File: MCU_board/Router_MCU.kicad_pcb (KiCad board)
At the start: 2 copper layers, 99 x 84.5 mm, 72 parts, among them J1 Header, T1 HY601742, U1 MYC-YT507H, U2 TPS54340, U3 LAN8720A, X1 B4B-XH, X2 B4B-XH, X3 B4B-XH, X4 B4B-XH, X5 B2B-XH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

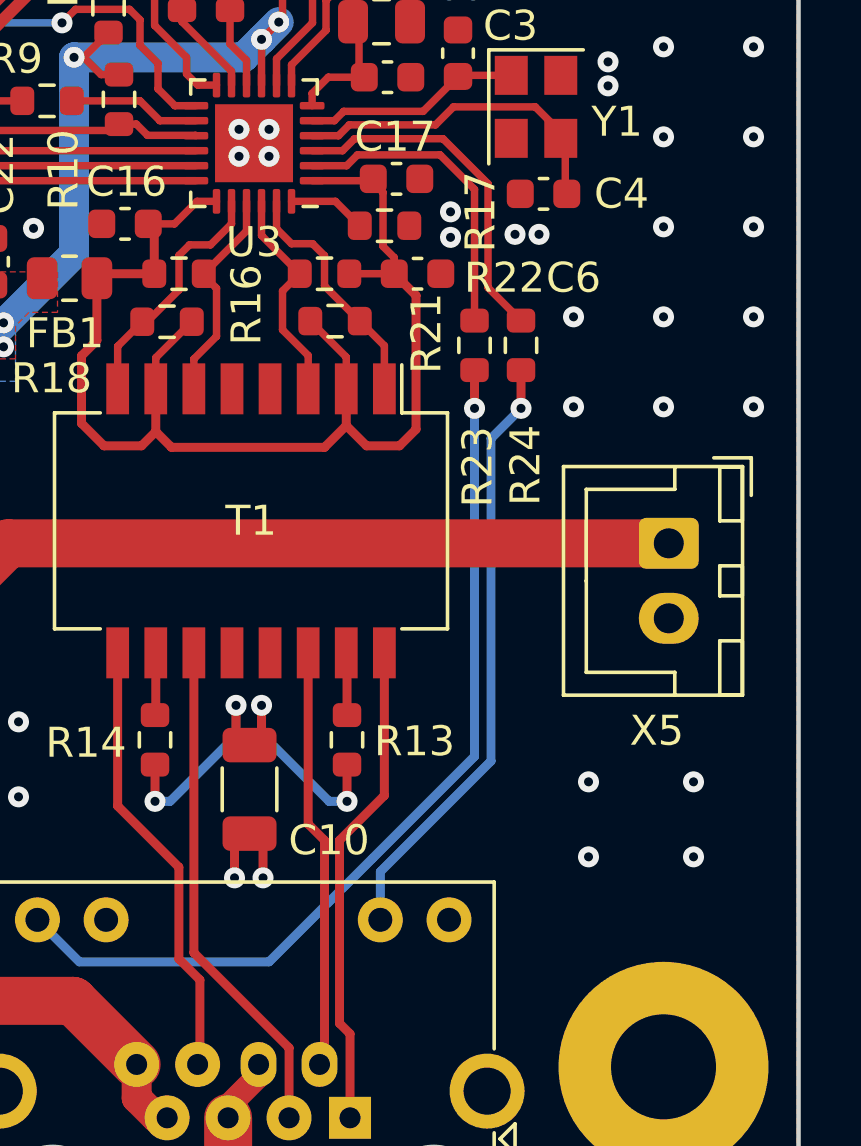
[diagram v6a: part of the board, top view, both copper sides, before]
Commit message: lan8720 led config resistor
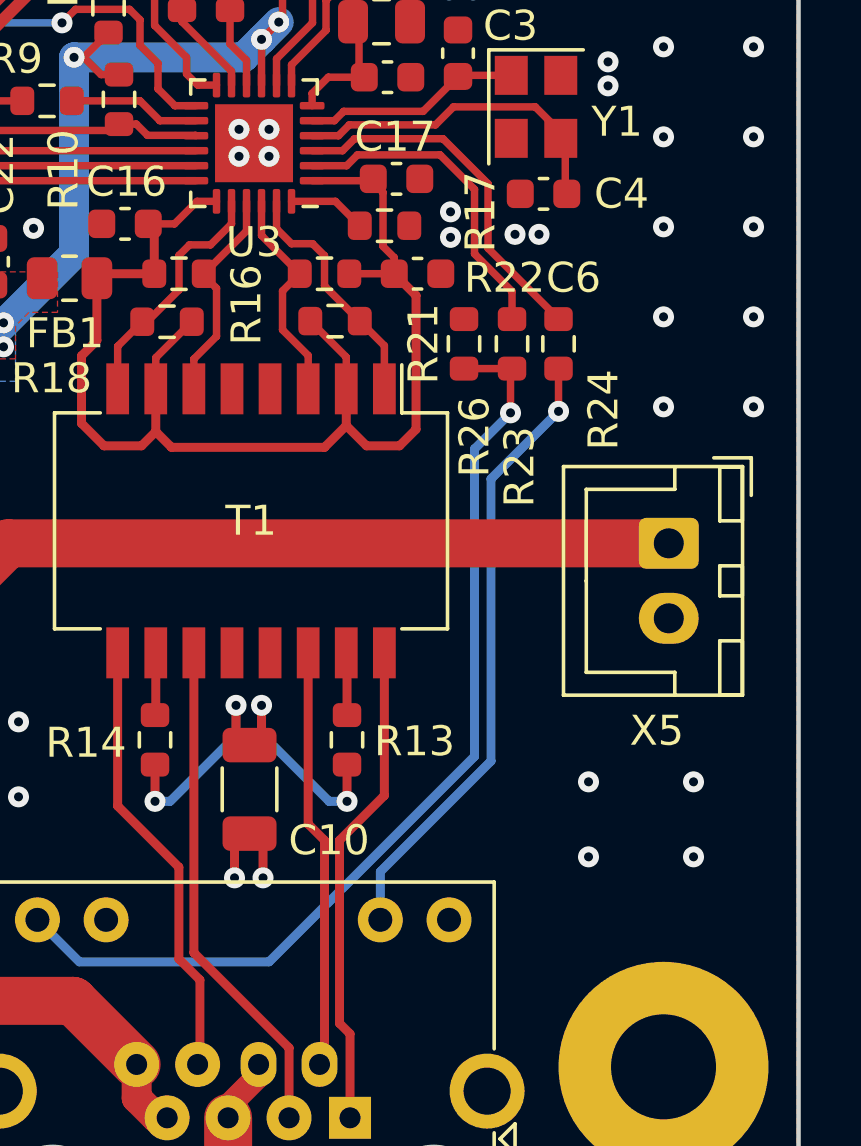
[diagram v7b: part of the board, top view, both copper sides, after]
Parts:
- added R26: 10k, Resistor_SMD:R_0603_1608Metric, F.Cu at (199.7, 122.8)
- moved R23 1.25 mm to (201.3, 122.8)
- moved R24 1.25 mm to (202.8, 122.8)
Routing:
- net Net-(R23-Pad1): track 30.9 -> 33.0 mm
- net Net-(R24-Pad1): track 20.3 -> 20.8 mm
- net GND: vias 223 -> 221
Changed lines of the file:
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@@
   )
   (footprint "Resistor_SMD:R_0603_1608Metric" (layer "F.Cu")
-    (at 201.6 122.8 90)
+    (at 202.85 122.75 90)
     (descr "Resistor SMD 0603 (1608 Metric), square (rectangular) end terminal, IPC_7351 nominal, (Body size source: IPC-SM-782 page 72, https://www.pcb-3d.com/wordpress/wp-content/uploads/ipc-sm-782a_amendment_1_and_2.pdf), generated with kicad-footprint-generator")
     (tags "resistor")
@@
     (property "Sheetname" "")
     (attr smd)
-    (fp_text reference "R24" (at -4 0.15 270) (layer "F.SilkS")
+    (fp_text reference "R24" (at -2.2 1.5 270) (layer "F.SilkS")
       (effects (font (size 1 1) (thickness 0.15)))
     )
@@
   )
   (footprint "Resistor_SMD:R_0603_1608Metric" (layer "F.Cu")
-    (at 200.05 122.8 90)
+    (at 201.3 122.75 90)
     (descr "Resistor SMD 0603 (1608 Metric), square (rectangular) end terminal, IPC_7351 nominal, (Body size source: IPC-SM-782 page 72, https://www.pcb-3d.com/wordpress/wp-content/uploads/ipc-sm-782a_amendment_1_and_2.pdf), generated with kicad-footprint-generator")
     (tags "resistor")
@@
     (property "Sheetname" "")
     (attr smd)
-    (fp_text reference "R23" (at -4.05 0.1 270) (layer "F.SilkS")
+    (fp_text reference "R23" (at -4.1 0.25 270) (layer "F.SilkS")
       (effects (font (size 1 1) (thickness 0.15)))
     )
@@
       (net 2 "GND") (pinfunction "1") (pintype "input"))
   )
+  (footprint "Resistor_SMD:R_0603_1608Metric" (layer "F.Cu")
+    (at 199.7 122.75 -90)
+    (descr "Resistor SMD 0603 (1608 Metric), square (rectangular) end terminal, IPC_7351 nominal, (Body size source: IPC-SM-782 page 72, https://www.pcb-3d.com/wordpress/wp-content/uploads/ipc-sm-782a_amendment_1_and_2.pdf), generated with kicad-footprint-generator")
+    (tags "resistor")
+    (property "Sheetfile" "Router_MCU.kicad_sch")
+    (property "Sheetname" "")
+    (attr smd)
+    (fp_text reference "R26" (at 3.1 -0.35 90) (layer "F.SilkS")
+      (effects (font (size 1 1) (thickness 0.15)))
+    )
+    (fp_text value "10k" (at 0 1.43 90) (layer "F.Fab")
+      (effects (font (size 1 1) (thickness 0.15)))
+    )
+    (fp_text user "${REFERENCE}" (at 0 0 90) (layer "F.Fab")
+      (effects (font (size 0.4 0.4) (thickness 0.06)))
+    )
+    (fp_line (start -0.237258 -0.5225) (end 0.237258 -0.5225) (layer "F.SilkS") (width 0.12))
+    (fp_line (start -0.237258 0.5225) (end 0.237258 0.5225) (layer "F.SilkS") (width 0.12))
+    (fp_line (start -1.48 0.73) (end -1.48 -0.73) (layer "F.CrtYd") (width 0.05))
+    (fp_line (start 1.48 0.73) (end -1.48 0.73) (layer "F.CrtYd") (width 0.05))
+    (fp_line (start 1.48 -0.73) (end 1.48 0.73) (layer "F.CrtYd") (width 0.05))
+    (fp_line (start -1.48 -0.73) (end 1.48 -0.73) (layer "F.CrtYd") (width 0.05))
+    (fp_line (start 0.8 0.4125) (end -0.8 0.4125) (layer "F.Fab") (width 0.1))
+    (fp_line (start 0.8 -0.4125) (end 0.8 0.4125) (layer "F.Fab") (width 0.1))
+    (fp_line (start -0.8 0.4125) (end -0.8 -0.4125) (layer "F.Fab") (width 0.1))
+    (fp_line (start -0.8 -0.4125) (end 0.8 -0.4125) (layer "F.Fab") (width 0.1))
+    (pad "1" smd roundrect (at -0.825 0 270) (size 0.8 0.95) (layers "F.Cu" "F.Paste" "F.Mask") (roundrect_rratio 0.25)
+      (net 2 "GND") (pintype "passive"))
+    (pad "2" smd roundrect (at 0.825 0 270) (size 0.8 0.95) (layers "F.Cu" "F.Paste" "F.Mask") (roundrect_rratio 0.25)
+      (net 44 "Net-(R23-Pad1)") (pintype "passive"))
+    (model "${KICAD6_3DMODEL_DIR}/Resistor_SMD.3dshapes/R_0603_1608Metric.wrl"
+      (offset (xyz 0 0 0))
+      (scale (xyz 1 1 1))
+      (rotate (xyz 0 0 0))
+    )
+  )
   (footprint "Capacitor_SMD:C_0603_1608Metric" (layer "F.Cu")
     (at 188.4 118.75 180)
@@
     (property "Sheetname" "")
     (attr smd)
-    (fp_text reference "R21" (at 3.05 0.4075 90) (layer "F.SilkS")
+    (fp_text reference "R21" (at 2.95 0.7575 90) (layer "F.SilkS")
       (effects (font (size 1 1) (thickness 0.15)))
     )
@@
   (via (at 204.5 113.35) (size 0.7) (drill 0.3) (layers "F.Cu" "B.Cu") (free) (net 2))
   (via (at 192.05 140.55) (size 0.7) (drill 0.3) (layers "F.Cu" "B.Cu") (net 2))
-  (via (at 203.35 124.85) (size 0.7) (drill 0.3) (layers "F.Cu" "B.Cu") (free) (net 2))
   (via (at 181.1 118.85) (size 0.7) (drill 0.3) (layers "F.Cu" "B.Cu") (free) (net 2))
   (via (at 134.85 140.35) (size 0.7) (drill 0.3) (layers "F.Cu" "B.Cu") (free) (net 2))
@@
   (via (at 179.85 151.35) (size 0.7) (drill 0.3) (layers "F.Cu" "B.Cu") (free) (net 2))
   (via (at 154.35 144.85) (size 0.7) (drill 0.3) (layers "F.Cu" "B.Cu") (free) (net 2))
-  (via (at 203.35 121.85) (size 0.7) (drill 0.3) (layers "F.Cu" "B.Cu") (free) (net 2))
   (via (at 114.35 131.35) (size 0.7) (drill 0.3) (layers "F.Cu" "B.Cu") (free) (net 2))
   (via (at 200 110.95) (size 0.7) (drill 0.3) (layers "F.Cu" "B.Cu") (free) (net 2))
@@
   (segment (start 193.65 122.284962) (end 194.505 123.139962) (width 0.25) (layer "F.Cu") (net 43))
   (segment (start 194.505 123.139962) (end 194.505 124.25) (width 0.25) (layer "F.Cu") (net 43))
-  (segment (start 200.05 124.9) (end 200.05 123.625) (width 0.3) (layer "F.Cu") (net 44))
-  (via (at 200.05 124.9) (size 0.7) (drill 0.3) (layers "F.Cu" "B.Cu") (net 44))
-  (segment (start 196.65 139.9) (end 200.05 136.5) (width 0.3) (layer "B.Cu") (net 44))
-  (segment (start 200.05 136.5) (end 200.05 124.9) (width 0.3) (layer "B.Cu") (net 44))
-  (segment (start 196.65 139.9) (end 193.2 143.35) (width 0.3) (layer "B.Cu") (net 44))
-  (segment (start 186.88 143.35) (end 185.48 141.95) (width 0.3) (layer "B.Cu") (net 44))
+  (segment (start 199.7 123.575) (end 201.3 123.575) (width 0.25) (layer "F.Cu") (net 44))
+  (segment (start 201.25 123.625) (end 201.3 123.575) (width 0.25) (layer "F.Cu") (net 44))
+  (segment (start 201.25 125.05) (end 201.25 123.625) (width 0.25) (layer "F.Cu") (net 44))
+  (via (at 201.25 125.05) (size 0.7) (drill 0.3) (layers "F.Cu" "B.Cu") (net 44))
+  (segment (start 200.05 136.5) (end 193.2 143.35) (width 0.3) (layer "B.Cu") (net 44))
+  (segment (start 200.05 126.25) (end 200.05 136.5) (width 0.3) (layer "B.Cu") (net 44))
+  (segment (start 201.25 125.05) (end 200.05 126.25) (width 0.3) (layer "B.Cu") (net 44))
   (segment (start 193.2 143.35) (end 186.88 143.35) (width 0.3) (layer "B.Cu") (net 44))
+  (segment (start 186.88 143.35) (end 185.48 141.95) (width 0.3) (layer "B.Cu") (net 44))
   (segment (start 196.15 116.45) (end 198.9 116.45) (width 0.25) (layer "F.Cu") (net 45))
-  (segment (start 200.05 117.6) (end 200.05 121.975) (width 0.25) (layer "F.Cu") (net 45))
-  (segment (start 198.9 116.45) (end 200.05 117.6) (width 0.25) (layer "F.Cu") (net 45))
-  (segment (start 195.7875 116.8125) (end 196.15 116.45) (width 0.25) (layer "F.Cu") (net 45))
   (segment (start 194.6375 116.8125) (end 195.7875 116.8125) (width 0.25) (layer "F.Cu") (net 45))
-  (segment (start 201.6 123.625) (end 201.6 124.9) (width 0.3) (layer "F.Cu") (net 46))
-  (via (at 201.6 124.9) (size 0.7) (drill 0.3) (layers "F.Cu" "B.Cu") (net 46))
-  (segment (start 196.91 140.347106) (end 196.91 141.95) (width 0.3) (layer "B.Cu") (net 46))
-  (segment (start 200.6 125.9) (end 200.6 136.657106) (width 0.3) (layer "B.Cu") (net 46))
+  (segment (start 200.05 117.6) (end 200.05 119.75) (width 0.25) (layer "F.Cu") (net 45))
+  (segment (start 201.3 121) (end 201.3 121.925) (width 0.25) (layer "F.Cu") (net 45))
+  (segment (start 195.7875 116.8125) (end 196.15 116.45) (width 0.25) (layer "F.Cu") (net 45))
+  (segment (start 200.05 119.75) (end 201.3 121) (width 0.25) (layer "F.Cu") (net 45))
+  (segment (start 198.9 116.45) (end 200.05 117.6) (width 0.25) (layer "F.Cu") (net 45))
+  (segment (start 202.85 123.575) (end 202.85 125) (width 0.25) (layer "F.Cu") (net 46))
+  (via (at 202.85 125) (size 0.7) (drill 0.3) (layers "F.Cu" "B.Cu") (net 46))
   (segment (start 200.6 136.657106) (end 196.91 140.347106) (width 0.3) (layer "B.Cu") (net 46))
-  (segment (start 201.6 124.9) (end 200.6 125.9) (width 0.3) (layer "B.Cu") (net 46))
-  (segment (start 200.5 117.413604) (end 200.5 120.875) (width 0.25) (layer "F.Cu") (net 47))
-  (segment (start 196.05 115.913604) (end 199 115.913604) (width 0.25) (layer "F.Cu") (net 47))
+  (segment (start 196.91 140.347106) (end 196.91 141.95) (width 0.3) (layer "B.Cu") (net 46))
+  (segment (start 202.85 125) (end 200.6 127.25) (width 0.3) (layer "B.Cu") (net 46))
+  (segment (start 200.6 127.25) (end 200.6 136.657106) (width 0.3) (layer "B.Cu") (net 46))
+  (segment (start 200.5 117.413604) (end 200.5 119.563604) (width 0.25) (layer "F.Cu") (net 47))
   (segment (start 195.651104 116.3125) (end 196.05 115.913604) (width 0.25) (layer "F.Cu") (net 47))
-  (segment (start 200.5 120.875) (end 201.6 121.975) (width 0.25) (layer "F.Cu") (net 47))
   (segment (start 199 115.913604) (end 200.5 117.413604) (width 0.25) (layer "F.Cu") (net 47))
   (segment (start 194.6375 116.3125) (end 195.651104 116.3125) (width 0.25) (layer "F.Cu") (net 47))
+  (segment (start 196.05 115.913604) (end 199 115.913604) (width 0.25) (layer "F.Cu") (net 47))
+  (segment (start 202.85 121.913604) (end 202.85 121.925) (width 0.25) (layer "F.Cu") (net 47))
+  (segment (start 200.5 119.563604) (end 202.85 121.913604) (width 0.25) (layer "F.Cu") (net 47))
   (segment (start 167.85 141.1) (end 167.85 138.475) (width 0.3) (layer "F.Cu") (net 48))
   (segment (start 149.4 134.95) (end 149.4 133.6) (width 0.3) (layer "F.Cu") (net 49))
